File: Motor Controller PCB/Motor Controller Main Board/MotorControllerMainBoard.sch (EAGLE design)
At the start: 86 parts, among them T1 TEENSY_3.1_ALL_PINS

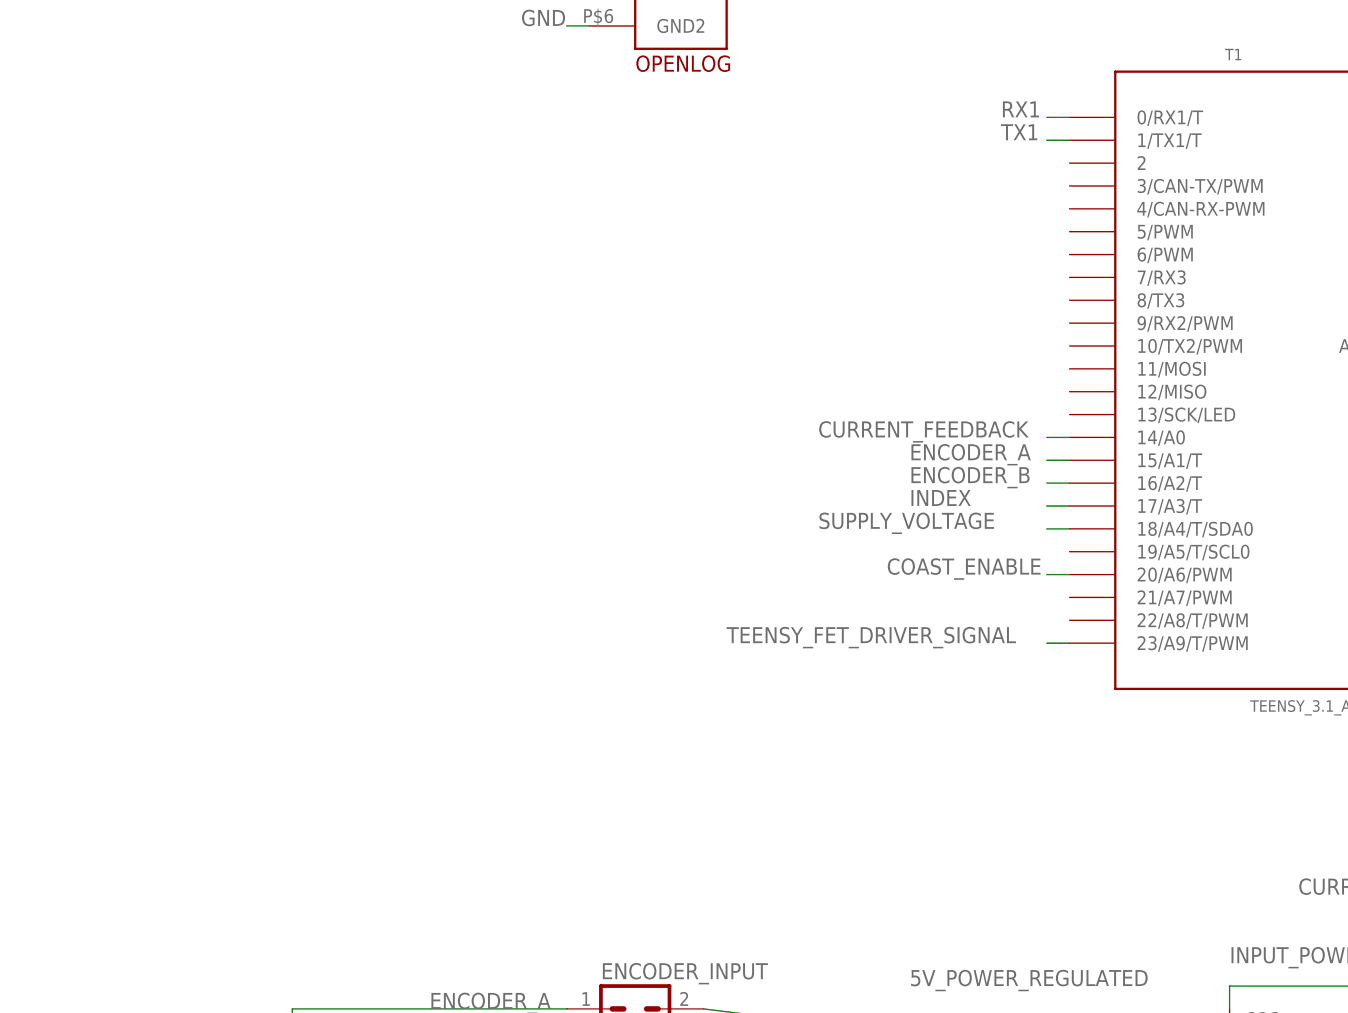
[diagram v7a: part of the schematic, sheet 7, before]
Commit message: Added digital connections
added digital connects, saving before routing them.
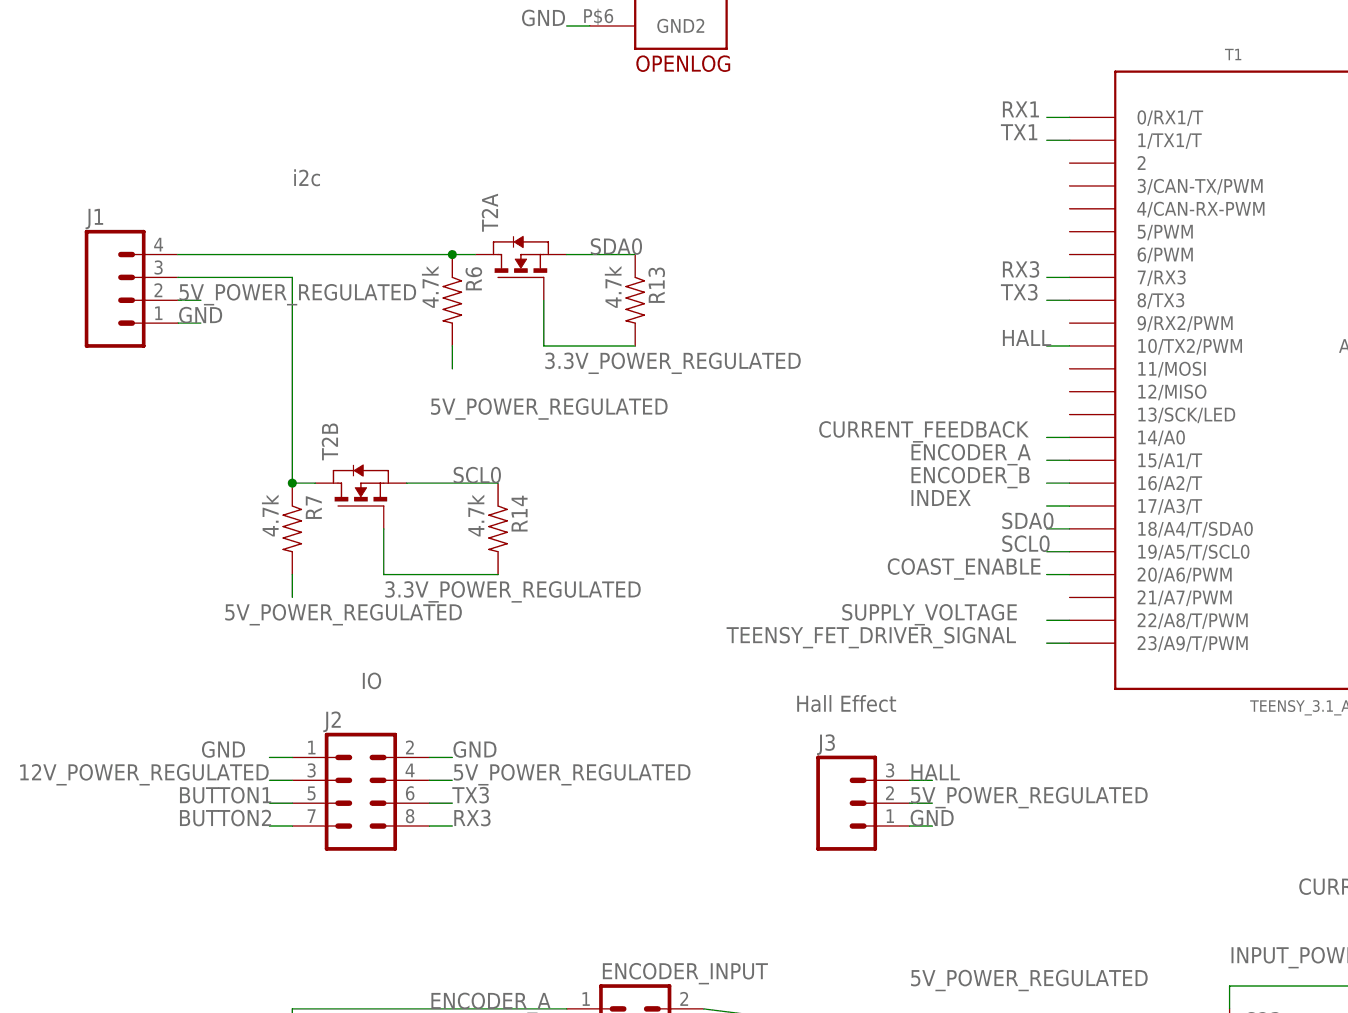
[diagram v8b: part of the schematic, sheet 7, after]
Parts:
- added J1: (no value), SparkFun-Connectors:M04PTH
- added J2: (no value), SparkFun-Connectors:M04X2
- added J3: (no value), SparkFun-Connectors:M03PTH
- added R13, R14, R6, R7: 4.7k, SparkFun-Passives:RESISTOR0805-RES
- added T2: (no value), zetex:NMOS2SO8
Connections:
- new net BUTTON1: J2.5
- new net BUTTON2: J2.7
- new net HALL: J3.3, T1.10/TX2/PWM
- new net N$19: J1.3, R7.1, T2B.D
- new net N$20: J1.4, R6.1, T2A.D
- new net RX3: J2.8, T1.7/RX3
- new net SCL0: R14.1, T1.19/A5/T/SCL0, T2B.S
- new net SDA0: R13.1, T1.18/A4/T/SDA0, T2A.S
- new net TX3: J2.6, T1.8/TX3
- net 12V_POWER_REGULATED: now also J2.3
- net 3.3V_POWER_REGULATED: now also R13.2, R14.2, T2A.G, T2B.G
- net 5V_POWER_REGULATED: now also J1.2, J2.4, J3.2, R6.2, R7.2
- net GND: now also J1.1, J2.1, J2.2, J3.1
- net SUPPLY_VOLTAGE: now also T1.22/A8/T/PWM; no longer T1.18/A4/T/SDA0
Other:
- note added: "Hall Effect"
- note added: "IO"
- note added: "i2c"
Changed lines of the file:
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@@
 <part name="GND33" library="E-P-008-R1.2" deviceset="GND" device=""/>
 <part name="L2" library="SparkFun (2015_10_14 22_27_04 UTC)" deviceset="INDUCTOR" device="0805" value="42nH"/>
+<part name="J1" library="SparkFun-Connectors" deviceset="M04" device="PTH"/>
+<part name="R6" library="SparkFun-Passives" deviceset="RESISTOR" device="0805-RES" value="4.7k"/>
+<part name="T2" library="zetex" library_urn="urn:adsk.eagle:library:418" deviceset="NMOS2" device="SO8" package3d_urn="urn:adsk.eagle:package:30987/1"/>
+<part name="R13" library="SparkFun-Passives" deviceset="RESISTOR" device="0805-RES" value="4.7k"/>
+<part name="R7" library="SparkFun-Passives" deviceset="RESISTOR" device="0805-RES" value="4.7k"/>
+<part name="R14" library="SparkFun-Passives" deviceset="RESISTOR" device="0805-RES" value="4.7k"/>
+<part name="J2" library="SparkFun-Connectors" deviceset="M04X2" device=""/>
+<part name="J3" library="SparkFun-Connectors" deviceset="M03" device="PTH"/>
 </parts>
 <sheets>
@@
 <text x="223.52" y="58.42" size="1.778" layer="91" rot="R270">Schottky</text>
 <text x="223.52" y="76.2" size="1.778" layer="91" rot="R270">Schottky</text>
+<text x="30.48" y="154.94" size="1.778" layer="95">i2c</text>
+<text x="38.1" y="99.06" size="1.778" layer="95">IO</text>
+<text x="86.36" y="96.52" size="1.778" layer="95">Hall Effect</text>
 </plain>
 <instances>
@@
 <instance part="GND33" gate="1" x="231.14" y="50.8"/>
 <instance part="L2" gate="G$1" x="208.28" y="144.78" rot="R90"/>
+<instance part="J1" gate="G$1" x="12.7" y="142.24"/>
+<instance part="R6" gate="G$1" x="48.26" y="142.24" rot="R270"/>
+<instance part="T2" gate="A" x="55.88" y="147.32" rot="R90"/>
+<instance part="T2" gate="B" x="38.1" y="121.92" rot="R90"/>
+<instance part="R13" gate="G$1" x="68.58" y="142.24" rot="R270"/>
+<instance part="R7" gate="G$1" x="30.48" y="116.84" rot="R270"/>
+<instance part="R14" gate="G$1" x="53.34" y="116.84" rot="R270"/>
+<instance part="J2" gate="G$1" x="38.1" y="86.36"/>
+<instance part="J3" gate="J$1" x="91.44" y="86.36"/>
 </instances>
 <busses>
@@
 <wire x1="231.14" y1="55.88" x2="231.14" y2="53.34" width="0.1524" layer="91"/>
 </segment>
+<segment>
+<pinref part="J1" gate="G$1" pin="1"/>
+<wire x1="17.78" y1="139.7" x2="20.32" y2="139.7" width="0.1524" layer="91"/>
+<label x="17.78" y="139.7" size="1.778" layer="95"/>
+</segment>
+<segment>
+<wire x1="45.72" y1="91.44" x2="48.26" y2="91.44" width="0.1524" layer="91"/>
+<label x="48.26" y="91.44" size="1.778" layer="95"/>
+<pinref part="J2" gate="G$1" pin="2"/>
+</segment>
+<segment>
+<wire x1="30.48" y1="91.44" x2="27.94" y2="91.44" width="0.1524" layer="91"/>
+<label x="20.32" y="91.44" size="1.778" layer="95"/>
+<pinref part="J2" gate="G$1" pin="1"/>
+</segment>
+<segment>
+<pinref part="J3" gate="J$1" pin="1"/>
+<wire x1="99.06" y1="83.82" x2="101.6" y2="83.82" width="0.1524" layer="91"/>
+<label x="99.06" y="83.82" size="1.778" layer="95"/>
+</segment>
 </net>
 <net name="5V_POWER_REGULATED" class="0">
@@
 <label x="71.12" y="40.64" size="1.778" layer="95"/>
 </segment>
+<segment>
+<pinref part="J1" gate="G$1" pin="2"/>
+<wire x1="17.78" y1="142.24" x2="20.32" y2="142.24" width="0.1524" layer="91"/>
+<label x="17.78" y="142.24" size="1.778" layer="95"/>
+</segment>
+<segment>
+<pinref part="R6" gate="G$1" pin="2"/>
+<wire x1="48.26" y1="137.16" x2="48.26" y2="134.62" width="0.1524" layer="91"/>
+<label x="45.72" y="129.54" size="1.778" layer="95"/>
+</segment>
+<segment>
+<pinref part="R7" gate="G$1" pin="2"/>
+<wire x1="30.48" y1="111.76" x2="30.48" y2="109.22" width="0.1524" layer="91"/>
+<label x="22.86" y="106.68" size="1.778" layer="95"/>
+</segment>
+<segment>
+<wire x1="45.72" y1="88.9" x2="48.26" y2="88.9" width="0.1524" layer="91"/>
+<label x="48.26" y="88.9" size="1.778" layer="95"/>
+<pinref part="J2" gate="G$1" pin="4"/>
+</segment>
+<segment>
+<pinref part="J3" gate="J$1" pin="2"/>
+<wire x1="99.06" y1="86.36" x2="101.6" y2="86.36" width="0.1524" layer="91"/>
+<label x="99.06" y="86.36" size="1.778" layer="95"/>
+</segment>
 </net>
 <net name="3.3V_POWER_REGULATED" class="0">
@@
 <wire x1="215.9" y1="144.78" x2="223.52" y2="144.78" width="0.1524" layer="91"/>
 <label x="223.52" y="144.78" size="1.778" layer="95"/>
+</segment>
+<segment>
+<pinref part="T2" gate="A" pin="G"/>
+<wire x1="58.42" y1="142.24" x2="58.42" y2="137.16" width="0.1524" layer="91"/>
+<pinref part="R13" gate="G$1" pin="2"/>
+<wire x1="68.58" y1="137.16" x2="58.42" y2="137.16" width="0.1524" layer="91"/>
+<label x="58.42" y="134.62" size="1.778" layer="95"/>
+</segment>
+<segment>
+<pinref part="T2" gate="B" pin="G"/>
+<wire x1="40.64" y1="116.84" x2="40.64" y2="111.76" width="0.1524" layer="91"/>
+<pinref part="R14" gate="G$1" pin="2"/>
+<wire x1="40.64" y1="111.76" x2="53.34" y2="111.76" width="0.1524" layer="91"/>
+<label x="40.64" y="109.22" size="1.778" layer="95"/>
 </segment>
 </net>
@@
 </segment>
 <segment>
-<pinref part="T1" gate="G$1" pin="18/A4/T/SDA0"/>
-<wire x1="116.84" y1="116.84" x2="114.3" y2="116.84" width="0.1524" layer="91"/>
-<label x="88.9" y="116.84" size="1.778" layer="95"/>
+<pinref part="T1" gate="G$1" pin="22/A8/T/PWM"/>
+<wire x1="116.84" y1="106.68" x2="114.3" y2="106.68" width="0.1524" layer="91"/>
+<label x="91.44" y="106.68" size="1.778" layer="95"/>
 </segment>
 </net>
@@
 <wire x1="198.12" y1="73.66" x2="200.66" y2="73.66" width="0.1524" layer="91"/>
 <label x="182.88" y="71.12" size="1.778" layer="95"/>
+</segment>
+<segment>
+<wire x1="30.48" y1="88.9" x2="27.94" y2="88.9" width="0.1524" layer="91"/>
+<label x="0" y="88.9" size="1.778" layer="95"/>
+<pinref part="J2" gate="G$1" pin="3"/>
 </segment>
 </net>
@@
 </segment>
 </net>
+<net name="SCL0" class="0">
+<segment>
+<pinref part="T1" gate="G$1" pin="19/A5/T/SCL0"/>
+<wire x1="116.84" y1="114.3" x2="114.3" y2="114.3" width="0.1524" layer="91"/>
+<label x="109.22" y="114.3" size="1.778" layer="95"/>
+</segment>
+<segment>
+<pinref part="T2" gate="B" pin="S"/>
+<pinref part="R14" gate="G$1" pin="1"/>
+<wire x1="43.18" y1="121.92" x2="53.34" y2="121.92" width="0.1524" layer="91"/>
+<label x="48.26" y="121.92" size="1.778" layer="95"/>
+</segment>
+</net>
+<net name="SDA0" class="0">
+<segment>
+<pinref part="T1" gate="G$1" pin="18/A4/T/SDA0"/>
+<wire x1="116.84" y1="116.84" x2="114.3" y2="116.84" width="0.1524" layer="91"/>
+<label x="109.22" y="116.84" size="1.778" layer="95"/>
+</segment>
+<segment>
+<pinref part="T2" gate="A" pin="S"/>
+<wire x1="60.96" y1="147.32" x2="68.58" y2="147.32" width="0.1524" layer="91"/>
+<pinref part="R13" gate="G$1" pin="1"/>
+<label x="63.5" y="147.32" size="1.778" layer="95"/>
+</segment>
+</net>
+<net name="N$19" class="0">
+<segment>
+<pinref part="J1" gate="G$1" pin="3"/>
+<wire x1="17.78" y1="144.78" x2="30.48" y2="144.78" width="0.1524" layer="91"/>
+<pinref part="R7" gate="G$1" pin="1"/>
+<wire x1="30.48" y1="144.78" x2="30.48" y2="121.92" width="0.1524" layer="91"/>
+<pinref part="T2" gate="B" pin="D"/>
+<wire x1="33.02" y1="121.92" x2="30.48" y2="121.92" width="0.1524" layer="91"/>
+<junction x="30.48" y="121.92"/>
+</segment>
+</net>
+<net name="N$20" class="0">
+<segment>
+<pinref part="T2" gate="A" pin="D"/>
+<pinref part="R6" gate="G$1" pin="1"/>
+<wire x1="50.8" y1="147.32" x2="48.26" y2="147.32" width="0.1524" layer="91"/>
+<pinref part="J1" gate="G$1" pin="4"/>
+<wire x1="48.26" y1="147.32" x2="17.78" y2="147.32" width="0.1524" layer="91"/>
+<junction x="48.26" y="147.32"/>
+</segment>
+</net>
+<net name="RX3" class="0">
+<segment>
+<pinref part="T1" gate="G$1" pin="7/RX3"/>
+<wire x1="116.84" y1="144.78" x2="114.3" y2="144.78" width="0.1524" layer="91"/>
+<label x="109.22" y="144.78" size="1.778" layer="95"/>
+</segment>
+<segment>
+<wire x1="45.72" y1="83.82" x2="48.26" y2="83.82" width="0.1524" layer="91"/>
+<label x="48.26" y="83.82" size="1.778" layer="95"/>
+<pinref part="J2" gate="G$1" pin="8"/>
+</segment>
+</net>
+<net name="TX3" class="0">
+<segment>
+<pinref part="T1" gate="G$1" pin="8/TX3"/>
+<wire x1="116.84" y1="142.24" x2="114.3" y2="142.24" width="0.1524" layer="91"/>
+<label x="109.22" y="142.24" size="1.778" layer="95"/>
+</segment>
+<segment>
+<wire x1="45.72" y1="86.36" x2="48.26" y2="86.36" width="0.1524" layer="91"/>
+<label x="48.26" y="86.36" size="1.778" layer="95"/>
+<pinref part="J2" gate="G$1" pin="6"/>
+</segment>
+</net>
+<net name="BUTTON1" class="0">
+<segment>
+<wire x1="30.48" y1="86.36" x2="27.94" y2="86.36" width="0.1524" layer="91"/>
+<label x="17.78" y="86.36" size="1.778" layer="95"/>
+<pinref part="J2" gate="G$1" pin="5"/>
+</segment>
+</net>
+<net name="BUTTON2" class="0">
+<segment>
+<wire x1="30.48" y1="83.82" x2="27.94" y2="83.82" width="0.1524" layer="91"/>
+<label x="17.78" y="83.82" size="1.778" layer="95"/>
+<pinref part="J2" gate="G$1" pin="7"/>
+</segment>
+</net>
+<net name="HALL" class="0">
+<segment>
+<pinref part="J3" gate="J$1" pin="3"/>
+<wire x1="99.06" y1="88.9" x2="101.6" y2="88.9" width="0.1524" layer="91"/>
+<label x="99.06" y="88.9" size="1.778" layer="95"/>
+</segment>
+<segment>
+<pinref part="T1" gate="G$1" pin="10/TX2/PWM"/>
+<wire x1="116.84" y1="137.16" x2="114.3" y2="137.16" width="0.1524" layer="91"/>
+<label x="109.22" y="137.16" size="1.778" layer="95"/>
+</segment>
+</net>
